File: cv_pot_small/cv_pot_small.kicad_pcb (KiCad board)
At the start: 2 copper layers, 24 x 17 mm, 13 parts, among them J1 I/O connector, U1 HT7550-1, U2 LMV321IDBVR

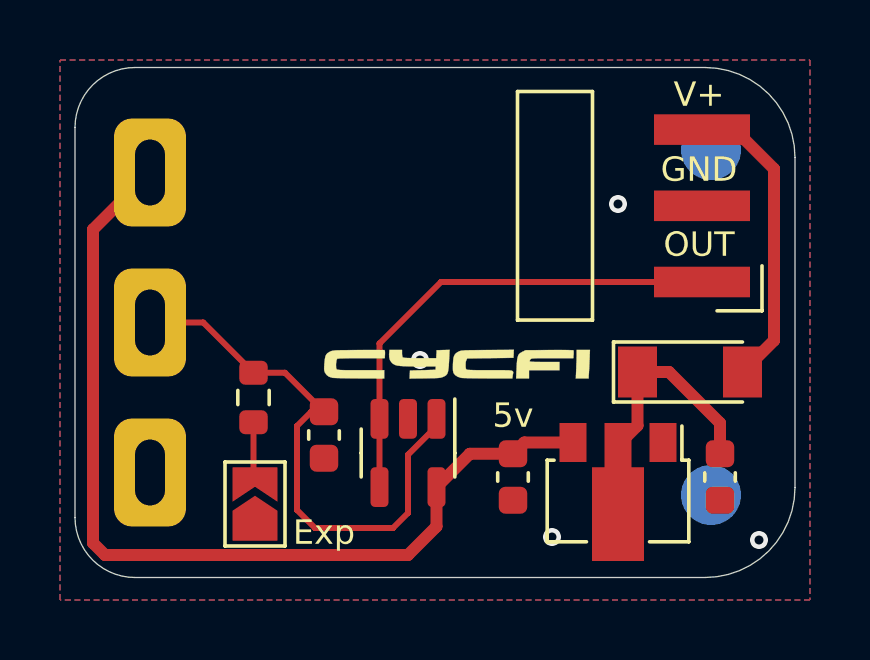
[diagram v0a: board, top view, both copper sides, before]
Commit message: Updated components for JLCPCB PCBA
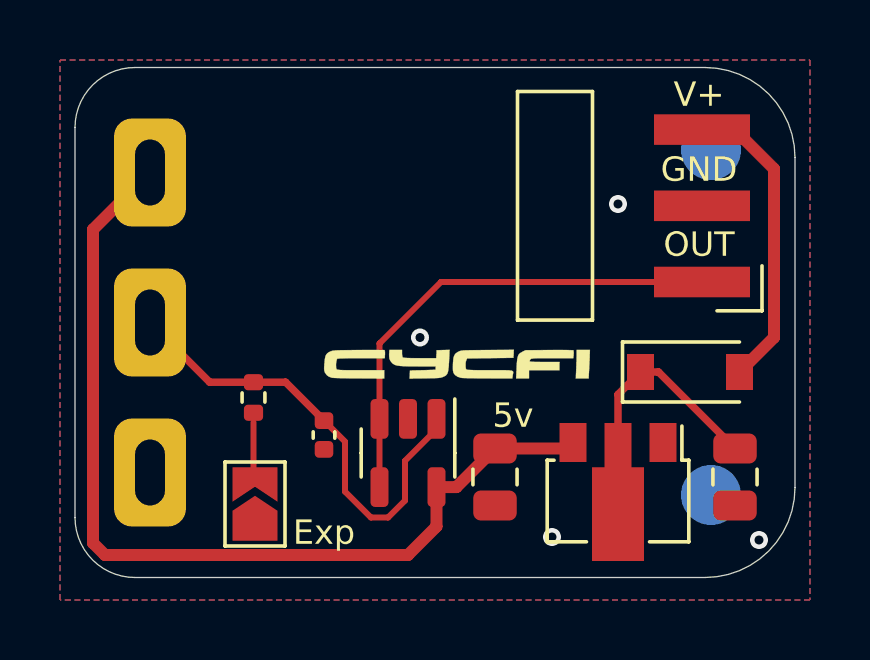
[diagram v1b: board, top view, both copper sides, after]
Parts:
- C1, C2: footprint Capacitor_SMD:C_0603_1608Metric -> Capacitor_SMD:C_0805_2012Metric
- C3: footprint Capacitor_SMD:C_0603_1608Metric -> Capacitor_SMD:C_0402_1005Metric
- D1: value LL4148 -> 1N4148W; footprint Diode_SMD:D_MiniMELF -> Diode_SMD:D_SOD-123
- R1: value 5k -> 4.7k; footprint Resistor_SMD:R_0603_1608Metric -> Resistor_SMD:R_0402_1005Metric
- moved C2 0.60 mm to (151.0, 85.7)
- moved C1 0.50 mm to (159.0, 85.7)
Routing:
- net /pot_center: track 18.6 -> 15.6 mm
